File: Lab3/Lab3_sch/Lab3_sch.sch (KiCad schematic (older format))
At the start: 8 parts

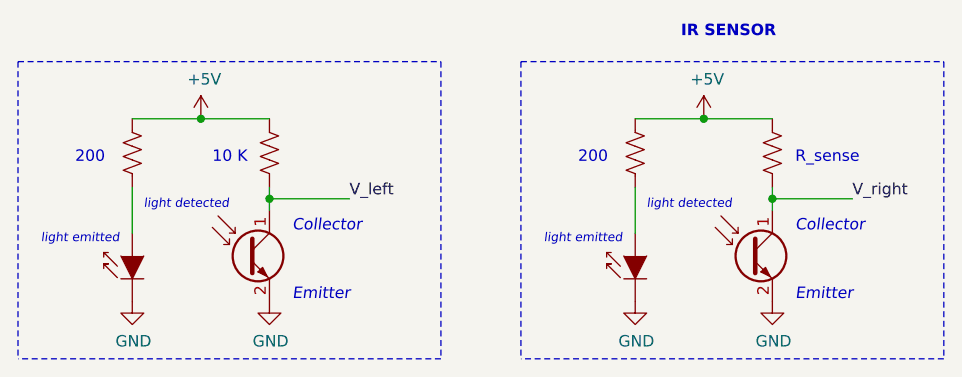
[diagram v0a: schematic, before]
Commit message: Final arduino code and python script for matlab fig.
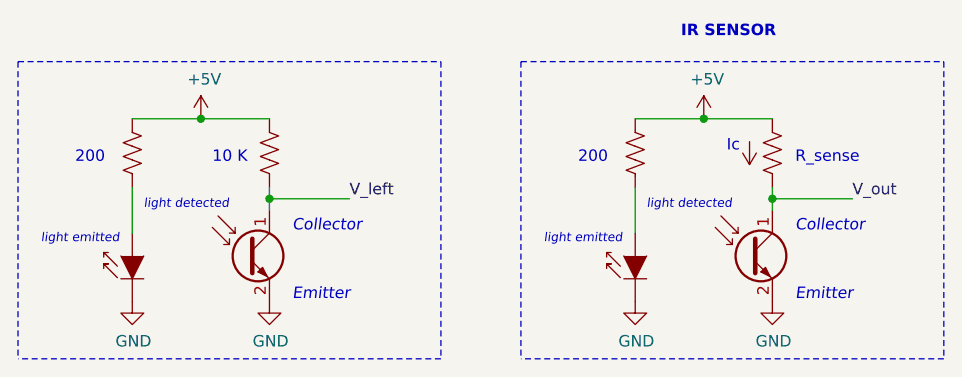
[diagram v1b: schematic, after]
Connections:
- net V_right renamed V_out
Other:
- note added: "Ic"
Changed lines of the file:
@@
 EESchema Schematic File Version 4
+LIBS:Lab3_sch-cache
 EELAYER 26 0
 EELAYER END
@@
 	650  2300 650  3600
 Text Label 4300 2900 0    50   ~ 0
-V_right
+V_out
 Text Notes 4050 3050 0    50   Italic 0
 Collector
@@
 Text Notes 3400 2950 0    39   Italic 0
 light detected
+$Comp
+L power:+5V #PWR?
+U 1 1 5DA22F4D
+P 3850 2650
+F 0 "#PWR?" H 3850 2500 50  0001 C CNN
+F 1 "+5V" H 4000 2700 50  0001 C CNN
+F 2 "" H 3850 2650 50  0001 C CNN
+F 3 "" H 3850 2650 50  0001 C CNN
+	1    3850 2650
+	-1   0    0    1
+$EndComp
+Text Notes 3750 2700 0    50   ~ 0
+Ic
 $EndSCHEMATC
